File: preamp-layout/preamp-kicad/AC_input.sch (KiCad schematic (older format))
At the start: 7 parts, among them J47 Screw_Terminal_01x02, J48 Screw_Terminal_01x02, P1 Conn_WallPlug, SW3 SW_SPST

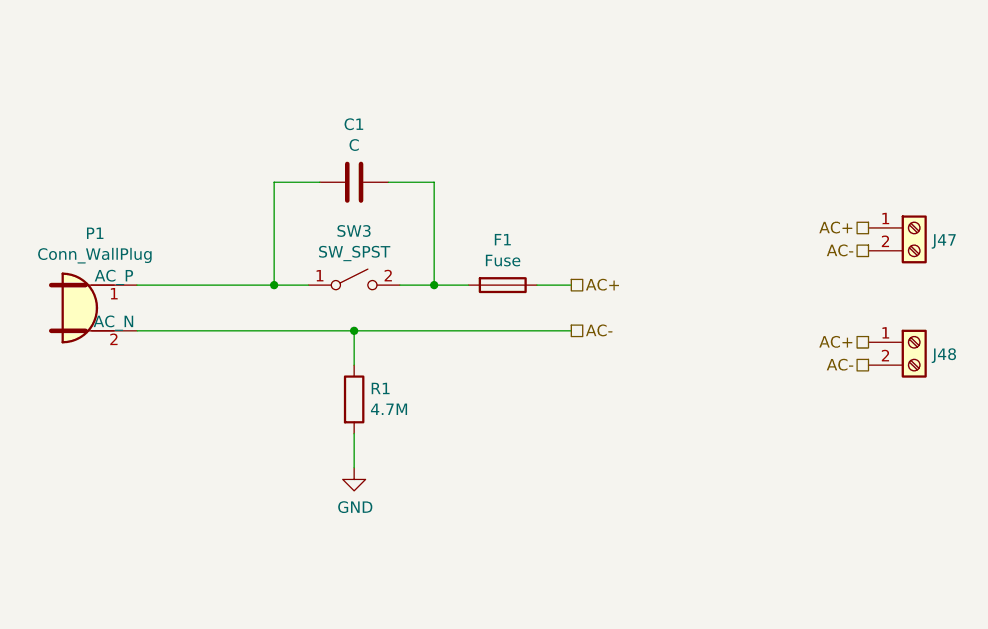
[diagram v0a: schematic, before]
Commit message: AC PCB Update
Removed Switch symbol from PCB, moved to main sheet. Started playing with footprint assignment. Other minor updates.
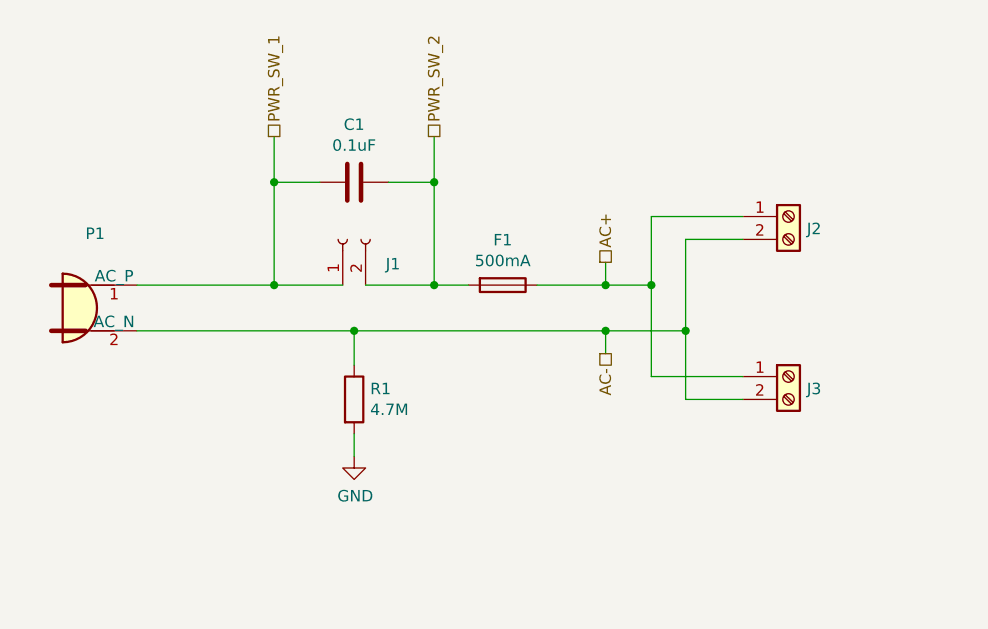
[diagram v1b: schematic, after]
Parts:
- removed SW3: SW_SPST, symbol Switch:SW_SPST
- added J1: Conn_01x02_Female, symbol Connector:Conn_01x02_Female
- C1: value C -> 0.1uF
- F1: value Fuse -> 500mA
- R1: footprint (none) -> Resistor_THT:R_Axial_DIN0207_L6.3mm_D2.5mm_P10.16mm_Horizontal
- renumbered J47 to J2, J48 to J3
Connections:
- net PWR_SW_1: now reaches C1.2, P1.1 (AC_P)
- net PWR_SW_1: now also J1.1 (Pin_1)
- net PWR_SW_2: now reaches C1.1, F1.2
- net PWR_SW_2: now also J1.2 (Pin_2)
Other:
- moved on the sheet: J2, J3
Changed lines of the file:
@@
 $EndDescr
-$Comp
-L Switch:SW_SPST SW3
-U 1 1 5E2C1E9A
-P 5250 3400
-F 0 "SW3" H 5250 3635 50  0000 C CNN
-F 1 "SW_SPST" H 5250 3544 50  0000 C CNN
-F 2 "" H 5250 3400 50  0001 C CNN
-F 3 "~" H 5250 3400 50  0001 C CNN
-	1    5250 3400
-	1    0    0    -1
-$EndComp
 $Comp
 L Device:C C1
@@
 P 5250 2950
 F 0 "C1" V 4998 2950 50  0000 C CNN
-F 1 "C" V 5089 2950 50  0000 C CNN
+F 1 "0.1uF" V 5089 2950 50  0000 C CNN
 F 2 "" H 5288 2800 50  0001 C CNN
 F 3 "~" H 5250 2950 50  0001 C CNN
@@
 $EndComp
 Wire Wire Line
-	5450 3400 5600 3400
-Wire Wire Line
 	4900 3400 4900 2950
 Wire Wire Line
 	4900 2950 5100 2950
-Wire Wire Line
-	4900 3400 5050 3400
 Wire Wire Line
 	5600 3400 5600 2950
@@
 P 5900 3400
 F 0 "F1" V 5703 3400 50  0000 C CNN
-F 1 "Fuse" V 5794 3400 50  0000 C CNN
+F 1 "500mA" V 5794 3400 50  0000 C CNN
 F 2 "" V 5830 3400 50  0001 C CNN
 F 3 "~" H 5900 3400 50  0001 C CNN
@@
 	5750 3400 5600 3400
 Connection ~ 5600 3400
-Text HLabel 6200 3400 2    50   UnSpc ~ 0
+Text HLabel 6350 3300 1    50   UnSpc ~ 0
 AC+
-Text HLabel 6200 3600 2    50   UnSpc ~ 0
+Text HLabel 6350 3700 3    50   UnSpc ~ 0
 AC-
-Wire Wire Line
-	6050 3400 6200 3400
 Wire Wire Line
 	5250 3750 5250 3600
@@
 F 0 "R1" H 5320 3946 50  0000 L CNN
 F 1 "4.7M" H 5320 3855 50  0000 L CNN
-F 2 "" V 5180 3900 50  0001 C CNN
+F 2 "Resistor_THT:R_Axial_DIN0207_L6.3mm_D2.5mm_P10.16mm_Horizontal" V 5180 3900 50  0001 C CNN
 F 3 "~" H 5250 3900 50  0001 C CNN
 	1    5250 3900
@@
 P 4100 3500
 F 0 "P1" H 4117 3825 50  0000 C CNN
-F 1 "Conn_WallPlug" H 4117 3734 50  0000 C CNN
+F 1 "Conn_WallPlug" H 4117 3734 50  0001 C CNN
 F 2 "" H 4500 3500 50  0001 C CNN
 F 3 "~" H 4500 3500 50  0001 C CNN
@@
 	1    0    0    -1
 $EndComp
-Wire Wire Line
-	5250 3600 6200 3600
 Wire Wire Line
 	4300 3600 5250 3600
@@
 L power:GND #PWR03
 U 1 1 649E3EA1
-P 5250 4200
-F 0 "#PWR03" H 5250 3950 50  0001 C CNN
-F 1 "GND" H 5255 4027 50  0000 C CNN
-F 2 "" H 5250 4200 50  0001 C CNN
-F 3 "" H 5250 4200 50  0001 C CNN
-	1    5250 4200
+P 5250 4150
+F 0 "#PWR03" H 5250 3900 50  0001 C CNN
+F 1 "GND" H 5255 3977 50  0000 C CNN
+F 2 "" H 5250 4150 50  0001 C CNN
+F 3 "" H 5250 4150 50  0001 C CNN
+	1    5250 4150
 	1    0    0    -1
 $EndComp
@@
 L Connector:Screw_Terminal_01x02 J?
 U 1 1 65B060F9
-P 7700 3150
+P 7150 3100
 AR Path="/5E27B612/65B060F9" Ref="J?"  Part="1"
-AR Path="/5E26F6FE/65B060F9" Ref="J47"  Part="1"
-F 0 "J47" H 7780 3096 50  0000 L CNN
-F 1 "Screw_Terminal_01x02" H 7780 3051 50  0001 L CNN
-F 2 "" H 7700 3150 50  0001 C CNN
-F 3 "~" H 7700 3150 50  0001 C CNN
-	1    7700 3150
+AR Path="/5E26F6FE/65B060F9" Ref="J2"  Part="1"
+F 0 "J2" H 7230 3046 50  0000 L CNN
+F 1 "Screw_Terminal_01x02" H 7230 3001 50  0001 L CNN
+F 2 "" H 7150 3100 50  0001 C CNN
+F 3 "~" H 7150 3100 50  0001 C CNN
+	1    7150 3100
 	1    0    0    -1
 $EndComp
-Text HLabel 7500 3150 0    50   UnSpc ~ 0
-AC+
-Text HLabel 7500 3250 0    50   UnSpc ~ 0
-AC-
 $Comp
 L Connector:Screw_Terminal_01x02 J?
 U 1 1 65B0680E
-P 7700 3650
+P 7150 3800
 AR Path="/5E27B612/65B0680E" Ref="J?"  Part="1"
-AR Path="/5E26F6FE/65B0680E" Ref="J48"  Part="1"
-F 0 "J48" H 7780 3596 50  0000 L CNN
-F 1 "Screw_Terminal_01x02" H 7780 3551 50  0001 L CNN
-F 2 "" H 7700 3650 50  0001 C CNN
-F 3 "~" H 7700 3650 50  0001 C CNN
-	1    7700 3650
+AR Path="/5E26F6FE/65B0680E" Ref="J3"  Part="1"
+F 0 "J3" H 7230 3746 50  0000 L CNN
+F 1 "Screw_Terminal_01x02" H 7230 3701 50  0001 L CNN
+F 2 "" H 7150 3800 50  0001 C CNN
+F 3 "~" H 7150 3800 50  0001 C CNN
+	1    7150 3800
 	1    0    0    -1
 $EndComp
-Text HLabel 7500 3650 0    50   UnSpc ~ 0
-AC+
-Text HLabel 7500 3750 0    50   UnSpc ~ 0
-AC-
+$Comp
+L Connector:Conn_01x02_Female J1
+U 1 1 5E2B212C
+P 5200 3200
+F 0 "J1" V 5092 3012 50  0000 R CNN
+F 1 "Conn_01x02_Female" V 5047 3012 50  0001 R CNN
+F 2 "" H 5200 3200 50  0001 C CNN
+F 3 "~" H 5200 3200 50  0001 C CNN
+	1    5200 3200
+	0    -1   -1   0
+$EndComp
 Wire Wire Line
-	5250 4050 5250 4200
+	5300 3400 5600 3400
+Wire Wire Line
+	4900 3400 5200 3400
+Wire Wire Line
+	5250 4050 5250 4150
+Wire Wire Line
+	6550 3400 6550 3100
+Wire Wire Line
+	6550 3100 6950 3100
+Wire Wire Line
+	6050 3400 6350 3400
+Wire Wire Line
+	6550 3400 6550 3800
+Wire Wire Line
+	6550 3800 6950 3800
+Connection ~ 6550 3400
+Wire Wire Line
+	6700 3600 6700 3200
+Wire Wire Line
+	6700 3200 6950 3200
+Wire Wire Line
+	5250 3600 6350 3600
+Wire Wire Line
+	6700 3600 6700 3900
+Wire Wire Line
+	6700 3900 6950 3900
+Connection ~ 6700 3600
+Wire Wire Line
+	6350 3300 6350 3400
+Connection ~ 6350 3400
+Wire Wire Line
+	6350 3400 6550 3400
+Wire Wire Line
+	6350 3700 6350 3600
+Connection ~ 6350 3600
+Wire Wire Line
+	6350 3600 6700 3600
+Text HLabel 4900 2750 1    50   UnSpc ~ 0
+PWR_SW_1
+Text HLabel 5600 2750 1    50   UnSpc ~ 0
+PWR_SW_2
+Wire Wire Line
+	4900 2750 4900 2950
+Connection ~ 4900 2950
+Wire Wire Line
+	5600 2750 5600 2950
+Connection ~ 5600 2950
 $EndSCHEMATC

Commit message: Initial Footprint Assignment
Assigned footprints to SMT resistors, pin headers, screw terminals, LEDs, DIP-8 ICs
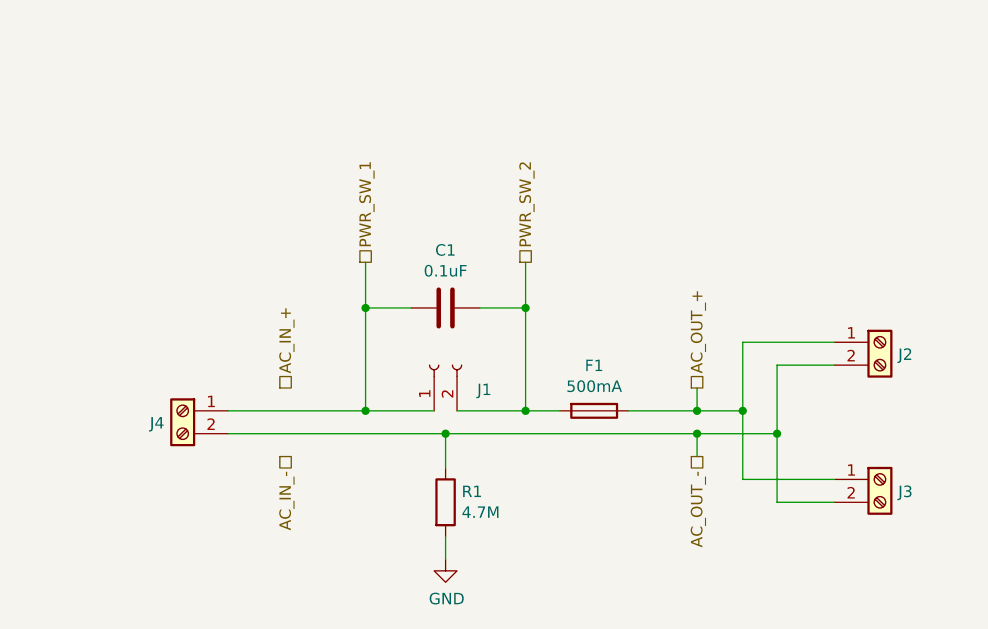
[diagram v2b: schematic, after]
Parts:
- removed P1: Conn_WallPlug, symbol Connector:Conn_WallPlug
- added J4: Screw_Terminal_01x02, TerminalBlock_Phoenix:TerminalBlock_Phoenix_PT-1,5-2-5.0-H_1x02_P5.00mm_Horizontal, symbol Connector:Screw_Terminal_01x02
- J1: footprint (none) -> Connector_PinHeader_2.54mm:PinHeader_1x02_P2.54mm_Vertical
- J2, J3: footprint (none) -> TerminalBlock_Phoenix:TerminalBlock_Phoenix_PT-1,5-2-5.0-H_1x02_P5.00mm_Horizontal
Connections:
- net PWR_SW_1: now also J4.1 (Pin_1)
- net AC+ renamed AC_OUT_+
- net AC- renamed AC_OUT_-
- net AC_OUT_-: now also J4.2 (Pin_2)
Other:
- moved on the sheet: C1, F1, J1, J2, J3, R1
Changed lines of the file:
@@
 L Device:C C1
 U 1 1 5E2C2703
-P 5250 2950
-F 0 "C1" V 4998 2950 50  0000 C CNN
-F 1 "0.1uF" V 5089 2950 50  0000 C CNN
-F 2 "" H 5288 2800 50  0001 C CNN
-F 3 "~" H 5250 2950 50  0001 C CNN
-	1    5250 2950
+P 5650 3500
+F 0 "C1" V 5398 3500 50  0000 C CNN
+F 1 "0.1uF" V 5489 3500 50  0000 C CNN
+F 2 "" H 5688 3350 50  0001 C CNN
+F 3 "~" H 5650 3500 50  0001 C CNN
+	1    5650 3500
 	0    1    1    0
 $EndComp
 Wire Wire Line
-	4900 3400 4900 2950
+	5300 3950 5300 3500
 Wire Wire Line
-	4900 2950 5100 2950
+	5300 3500 5500 3500
 Wire Wire Line
-	5600 3400 5600 2950
+	6000 3950 6000 3500
 Wire Wire Line
-	5600 2950 5400 2950
+	6000 3500 5800 3500
 $Comp
 L Device:Fuse F1
 U 1 1 5F91375A
-P 5900 3400
-F 0 "F1" V 5703 3400 50  0000 C CNN
-F 1 "500mA" V 5794 3400 50  0000 C CNN
-F 2 "" V 5830 3400 50  0001 C CNN
-F 3 "~" H 5900 3400 50  0001 C CNN
-	1    5900 3400
+P 6300 3950
+F 0 "F1" V 6103 3950 50  0000 C CNN
+F 1 "500mA" V 6194 3950 50  0000 C CNN
+F 2 "" V 6230 3950 50  0001 C CNN
+F 3 "~" H 6300 3950 50  0001 C CNN
+	1    6300 3950
 	0    1    1    0
 $EndComp
 Wire Wire Line
-	5750 3400 5600 3400
-Connection ~ 5600 3400
-Text HLabel 6350 3300 1    50   UnSpc ~ 0
-AC+
-Text HLabel 6350 3700 3    50   UnSpc ~ 0
-AC-
+	6150 3950 6000 3950
+Connection ~ 6000 3950
+Text HLabel 6750 3850 1    50   UnSpc ~ 0
+AC_OUT_+
+Text HLabel 6750 4150 3    50   UnSpc ~ 0
+AC_OUT_-
 Wire Wire Line
-	5250 3750 5250 3600
+	5650 4200 5650 4050
 $Comp
 L Device:R R1
 U 1 1 5E2C3357
-P 5250 3900
-F 0 "R1" H 5320 3946 50  0000 L CNN
-F 1 "4.7M" H 5320 3855 50  0000 L CNN
-F 2 "Resistor_THT:R_Axial_DIN0207_L6.3mm_D2.5mm_P10.16mm_Horizontal" V 5180 3900 50  0001 C CNN
-F 3 "~" H 5250 3900 50  0001 C CNN
-	1    5250 3900
-	1    0    0    -1
-$EndComp
-$Comp
-L Connector:Conn_WallPlug P1
-U 1 1 649DDD59
-P 4100 3500
-F 0 "P1" H 4117 3825 50  0000 C CNN
-F 1 "Conn_WallPlug" H 4117 3734 50  0001 C CNN
-F 2 "" H 4500 3500 50  0001 C CNN
-F 3 "~" H 4500 3500 50  0001 C CNN
-	1    4100 3500
+P 5650 4350
+F 0 "R1" H 5720 4396 50  0000 L CNN
+F 1 "4.7M" H 5720 4305 50  0000 L CNN
+F 2 "Resistor_THT:R_Axial_DIN0207_L6.3mm_D2.5mm_P10.16mm_Horizontal" V 5580 4350 50  0001 C CNN
+F 3 "~" H 5650 4350 50  0001 C CNN
+	1    5650 4350
 	1    0    0    -1
 $EndComp
 Wire Wire Line
-	4300 3600 5250 3600
-Connection ~ 5250 3600
+	4700 4050 5650 4050
+Connection ~ 5650 4050
 Wire Wire Line
-	4900 3400 4300 3400
-Connection ~ 4900 3400
+	5300 3950 4700 3950
+Connection ~ 5300 3950
 $Comp
 L power:GND #PWR03
 U 1 1 649E3EA1
-P 5250 4150
-F 0 "#PWR03" H 5250 3900 50  0001 C CNN
-F 1 "GND" H 5255 3977 50  0000 C CNN
-F 2 "" H 5250 4150 50  0001 C CNN
-F 3 "" H 5250 4150 50  0001 C CNN
-	1    5250 4150
+P 5650 4600
+F 0 "#PWR03" H 5650 4350 50  0001 C CNN
+F 1 "GND" H 5655 4427 50  0000 C CNN
+F 2 "" H 5650 4600 50  0001 C CNN
+F 3 "" H 5650 4600 50  0001 C CNN
+	1    5650 4600
 	1    0    0    -1
 $EndComp
@@
 L Connector:Screw_Terminal_01x02 J?
 U 1 1 65B060F9
-P 7150 3100
+P 7550 3650
 AR Path="/5E27B612/65B060F9" Ref="J?"  Part="1"
 AR Path="/5E26F6FE/65B060F9" Ref="J2"  Part="1"
-F 0 "J2" H 7230 3046 50  0000 L CNN
-F 1 "Screw_Terminal_01x02" H 7230 3001 50  0001 L CNN
-F 2 "" H 7150 3100 50  0001 C CNN
-F 3 "~" H 7150 3100 50  0001 C CNN
-	1    7150 3100
+F 0 "J2" H 7630 3596 50  0000 L CNN
+F 1 "Screw_Terminal_01x02" H 7630 3551 50  0001 L CNN
+F 2 "TerminalBlock_Phoenix:TerminalBlock_Phoenix_PT-1,5-2-5.0-H_1x02_P5.00mm_Horizontal" H 7550 3650 50  0001 C CNN
+F 3 "~" H 7550 3650 50  0001 C CNN
+	1    7550 3650
 	1    0    0    -1
 $EndComp
@@
 L Connector:Screw_Terminal_01x02 J?
 U 1 1 65B0680E
-P 7150 3800
+P 7550 4250
 AR Path="/5E27B612/65B0680E" Ref="J?"  Part="1"
 AR Path="/5E26F6FE/65B0680E" Ref="J3"  Part="1"
-F 0 "J3" H 7230 3746 50  0000 L CNN
-F 1 "Screw_Terminal_01x02" H 7230 3701 50  0001 L CNN
-F 2 "" H 7150 3800 50  0001 C CNN
-F 3 "~" H 7150 3800 50  0001 C CNN
-	1    7150 3800
+F 0 "J3" H 7630 4196 50  0000 L CNN
+F 1 "Screw_Terminal_01x02" H 7630 4151 50  0001 L CNN
+F 2 "TerminalBlock_Phoenix:TerminalBlock_Phoenix_PT-1,5-2-5.0-H_1x02_P5.00mm_Horizontal" H 7550 4250 50  0001 C CNN
+F 3 "~" H 7550 4250 50  0001 C CNN
+	1    7550 4250
 	1    0    0    -1
 $EndComp
@@
 L Connector:Conn_01x02_Female J1
 U 1 1 5E2B212C
-P 5200 3200
-F 0 "J1" V 5092 3012 50  0000 R CNN
-F 1 "Conn_01x02_Female" V 5047 3012 50  0001 R CNN
-F 2 "" H 5200 3200 50  0001 C CNN
-F 3 "~" H 5200 3200 50  0001 C CNN
-	1    5200 3200
+P 5600 3750
+F 0 "J1" V 5492 3562 50  0000 R CNN
+F 1 "Conn_01x02_Female" V 5447 3562 50  0001 R CNN
+F 2 "Connector_PinHeader_2.54mm:PinHeader_1x02_P2.54mm_Vertical" H 5600 3750 50  0001 C CNN
+F 3 "~" H 5600 3750 50  0001 C CNN
+	1    5600 3750
 	0    -1   -1   0
 $EndComp
 Wire Wire Line
-	5300 3400 5600 3400
+	5700 3950 6000 3950
 Wire Wire Line
-	4900 3400 5200 3400
+	5300 3950 5600 3950
 Wire Wire Line
-	5250 4050 5250 4150
+	5650 4500 5650 4600
 Wire Wire Line
-	6550 3400 6550 3100
+	6950 3950 6950 3650
 Wire Wire Line
-	6550 3100 6950 3100
+	6950 3650 7350 3650
 Wire Wire Line
-	6050 3400 6350 3400
+	6450 3950 6750 3950
 Wire Wire Line
-	6550 3400 6550 3800
+	7100 3750 7350 3750
 Wire Wire Line
-	6550 3800 6950 3800
-Connection ~ 6550 3400
+	5650 4050 6750 4050
 Wire Wire Line
-	6700 3600 6700 3200
+	6750 3850 6750 3950
+Connection ~ 6750 3950
 Wire Wire Line
-	6700 3200 6950 3200
+	6750 3950 6950 3950
 Wire Wire Line
-	5250 3600 6350 3600
+	6750 4150 6750 4050
+Connection ~ 6750 4050
 Wire Wire Line
-	6700 3600 6700 3900
-Wire Wire Line
-	6700 3900 6950 3900
-Connection ~ 6700 3600
-Wire Wire Line
-	6350 3300 6350 3400
-Connection ~ 6350 3400
-Wire Wire Line
-	6350 3400 6550 3400
-Wire Wire Line
-	6350 3700 6350 3600
-Connection ~ 6350 3600
-Wire Wire Line
-	6350 3600 6700 3600
-Text HLabel 4900 2750 1    50   UnSpc ~ 0
+	6750 4050 7100 4050
+Text HLabel 5300 3300 1    50   UnSpc ~ 0
 PWR_SW_1
-Text HLabel 5600 2750 1    50   UnSpc ~ 0
+Text HLabel 6000 3300 1    50   UnSpc ~ 0
 PWR_SW_2
 Wire Wire Line
-	4900 2750 4900 2950
-Connection ~ 4900 2950
+	5300 3300 5300 3500
+Connection ~ 5300 3500
 Wire Wire Line
-	5600 2750 5600 2950
-Connection ~ 5600 2950
+	6000 3300 6000 3500
+Connection ~ 6000 3500
+Text HLabel 4950 3850 1    50   UnSpc ~ 0
+AC_IN_+
+Text HLabel 4950 4150 3    50   UnSpc ~ 0
+AC_IN_-
+$Comp
+L Connector:Screw_Terminal_01x02 J?
+U 1 1 5E330384
+P 4500 3950
+AR Path="/5E27B612/5E330384" Ref="J?"  Part="1"
+AR Path="/5E26F6FE/5E330384" Ref="J4"  Part="1"
+F 0 "J4" H 4580 3896 50  0000 L CNN
+F 1 "Screw_Terminal_01x02" H 4580 3851 50  0001 L CNN
+F 2 "TerminalBlock_Phoenix:TerminalBlock_Phoenix_PT-1,5-2-5.0-H_1x02_P5.00mm_Horizontal" H 4500 3950 50  0001 C CNN
+F 3 "~" H 4500 3950 50  0001 C CNN
+	1    4500 3950
+	-1   0    0    -1
+$EndComp
+Wire Wire Line
+	7100 4050 7100 3750
+Wire Wire Line
+	6950 3950 6950 4250
+Wire Wire Line
+	6950 4250 7350 4250
+Connection ~ 6950 3950
+Wire Wire Line
+	7100 4050 7100 4350
+Wire Wire Line
+	7100 4350 7350 4350
+Connection ~ 7100 4050
 $EndSCHEMATC

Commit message: BOM update
Minor changes to schematic, value changes and footprint entry. BOM updated with parts sourcing
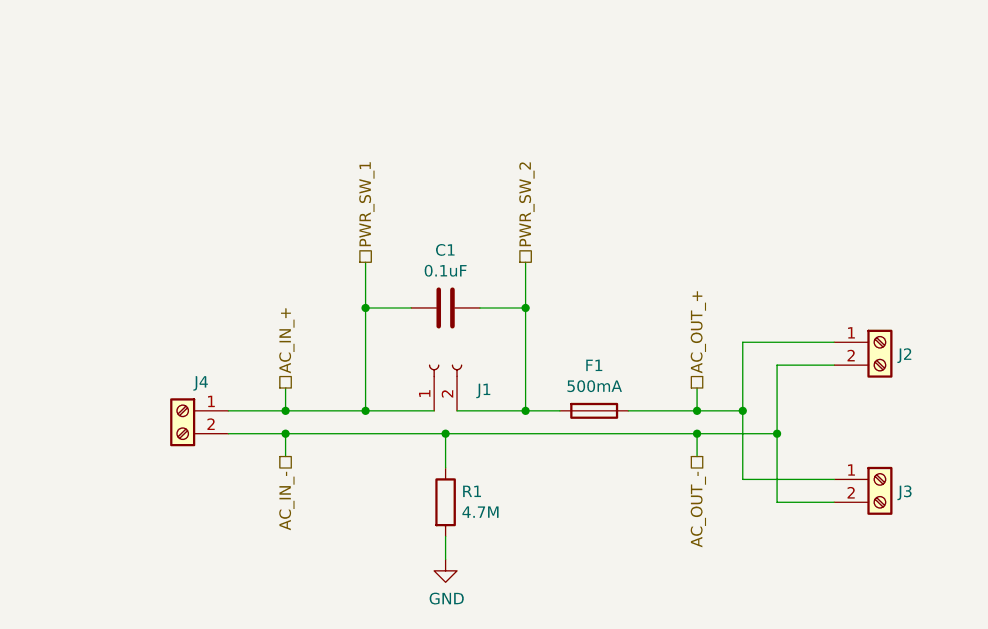
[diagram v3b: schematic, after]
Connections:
- net AC_OUT_- is gone; now on net AC_IN_-: J2.2 (Pin_2), J3.2 (Pin_2), J4.2 (Pin_2), R1.1
- net PWR_SW_1 is gone; now on net AC_IN_+: C1.2, J1.1 (Pin_1), J4.1 (Pin_1)
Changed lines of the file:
@@
 $EndComp
 Wire Wire Line
-	4700 4050 5650 4050
+	4700 4050 4950 4050
 Connection ~ 5650 4050
 Wire Wire Line
-	5300 3950 4700 3950
+	5300 3950 4950 3950
 Connection ~ 5300 3950
 $Comp
@@
 AR Path="/5E27B612/5E330384" Ref="J?"  Part="1"
 AR Path="/5E26F6FE/5E330384" Ref="J4"  Part="1"
-F 0 "J4" H 4580 3896 50  0000 L CNN
+F 0 "J4" H 4418 4075 50  0000 C CNN
 F 1 "Screw_Terminal_01x02" H 4580 3851 50  0001 L CNN
 F 2 "TerminalBlock_Phoenix:TerminalBlock_Phoenix_PT-1,5-2-5.0-H_1x02_P5.00mm_Horizontal" H 4500 3950 50  0001 C CNN
@@
 	7100 4350 7350 4350
 Connection ~ 7100 4050
+Wire Wire Line
+	4950 3850 4950 3950
+Connection ~ 4950 3950
+Wire Wire Line
+	4950 3950 4700 3950
+Wire Wire Line
+	4950 4150 4950 4050
+Connection ~ 4950 4050
+Wire Wire Line
+	4950 4050 5650 4050
 $EndSCHEMATC

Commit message: power headers updated, slight BOM update
changed footprint on all 5V, +-15V to JST B2B / B3B connectors. All male conns now.
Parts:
- J1: footprint Connector_PinHeader_2.54mm:PinHeader_1x02_P2.54mm_Vertical -> Connector_JST:JST_EH_B2B-EH-A_1x02_P2.50mm_Vertical
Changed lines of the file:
@@
 F 0 "J1" V 5492 3562 50  0000 R CNN
 F 1 "Conn_01x02_Female" V 5447 3562 50  0001 R CNN
-F 2 "Connector_PinHeader_2.54mm:PinHeader_1x02_P2.54mm_Vertical" H 5600 3750 50  0001 C CNN
+F 2 "Connector_JST:JST_EH_B2B-EH-A_1x02_P2.50mm_Vertical" H 5600 3750 50  0001 C CNN
 F 3 "~" H 5600 3750 50  0001 C CNN
 	1    5600 3750
